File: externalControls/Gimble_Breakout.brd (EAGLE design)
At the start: 33 x 41.6 mm, 5 parts

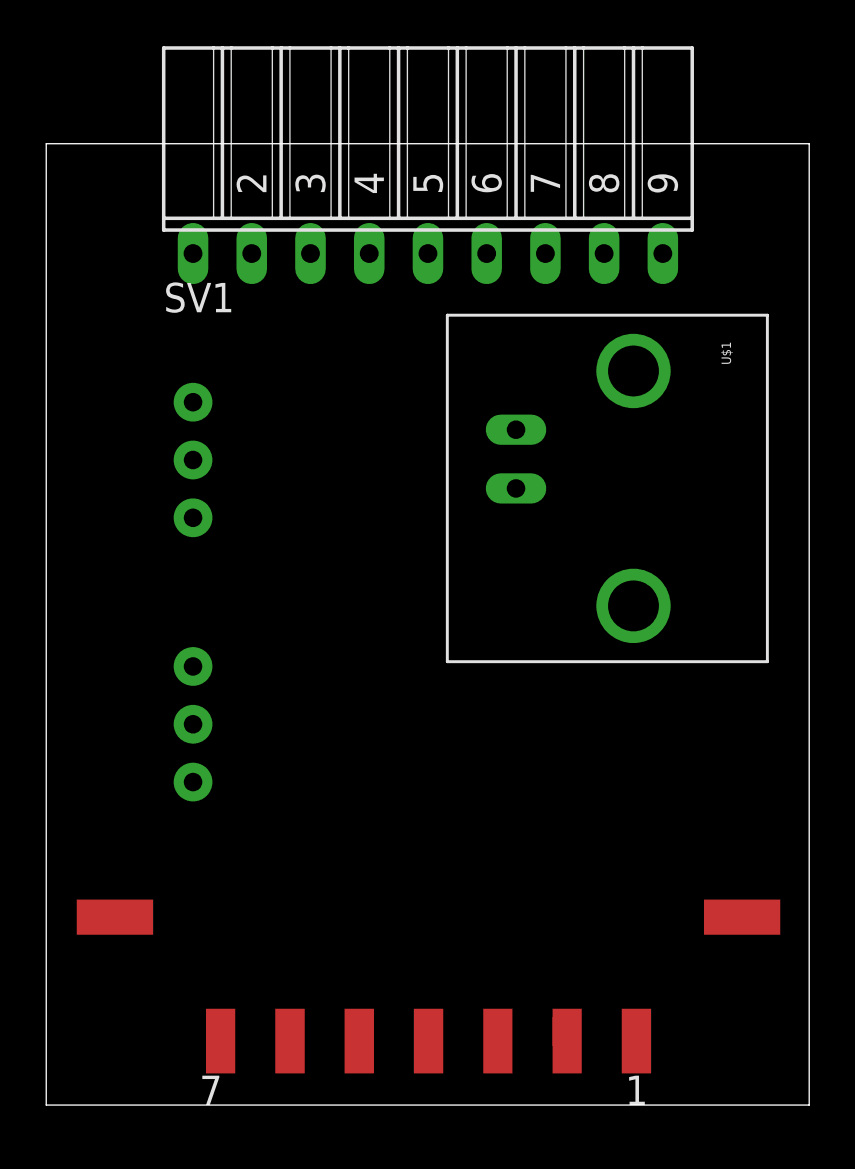
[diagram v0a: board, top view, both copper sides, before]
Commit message: Updated Routing
optimized a few paths
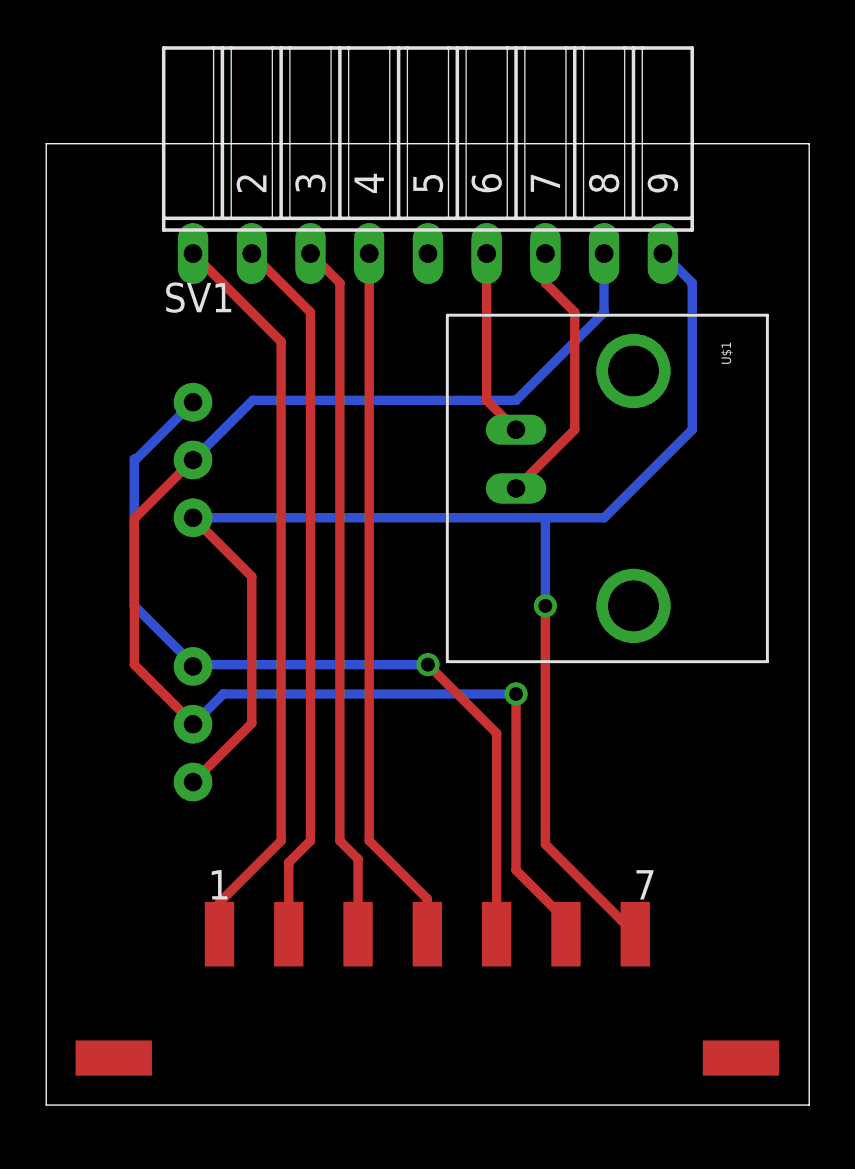
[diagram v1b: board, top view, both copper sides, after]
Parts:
- moved U$2 31.4 mm to (0.00, 59.7), turned to 0 degrees
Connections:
- net +12V: now also U$2.6
- net CAM_PWM0: now also U$2.4
- net CAM_PWM1: now also U$2.3
- net CAM_PWM2: now also U$2.2
- net CAM_PWM3: now also U$2.PAD1
- net DYNA_DATA: now also U$2.5
- net GND: now also U$2.7
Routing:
- net GND: track 0.00 -> 64.5 mm, vias 0 -> 1
- net +12V: track 0.00 -> 62.3 mm, vias 0 -> 1
- net DYNA_DATA: track 0.00 -> 36.7 mm, vias 0 -> 1
- net CAM_PWM3: track 0.00 -> 32.1 mm
- net CAM_PWM2: track 0.00 -> 30.9 mm
- net CAM_PWM0: track 0.00 -> 30.5 mm
- net CAM_PWM1: track 0.00 -> 30.3 mm
- net CAM_VIDEO: track 0.00 -> 11.7 mm
- net CAM_VIDEO_GND: track 0.00 -> 8.15 mm
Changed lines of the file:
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@@
 </element>
 <element name="U$1" library="SparkFun-Connectors" package="BNC" value="BNCPTH" x="19.05" y="85.09" rot="R270"/>
-<element name="U$2" library="logicShifter" package="MOLEX7PIN" value="MOLEX7-PIN" x="30.48" y="67.31" rot="R180"/>
+<element name="U$2" library="logicShifter" package="MOLEX7PIN" value="MOLEX7-PIN" x="0" y="59.69">
+<attribute name="TEST" value="1" x="0" y="59.69" size="1.778" layer="27" display="off"/>
+</element>
 </elements>
 <signals>
@@
 <contactref element="DYNA1" pad="P$1"/>
 <contactref element="SV1" pad="9"/>
-<wire x1="5.08" y1="83.82" x2="25.4" y2="95.25" width="0" layer="19" extent="1-1"/>
-<wire x1="5.08" y1="72.39" x2="5.08" y2="83.82" width="0" layer="19" extent="1-1"/>
+<contactref element="U$2" pad="7"/>
+<wire x1="5.08" y1="83.82" x2="7.62" y2="81.28" width="0.4064" layer="1"/>
+<wire x1="7.62" y1="81.28" x2="7.62" y2="74.93" width="0.4064" layer="1"/>
+<wire x1="7.62" y1="74.93" x2="5.08" y2="72.39" width="0.4064" layer="1"/>
+<wire x1="25.4" y1="95.25" x2="26.67" y2="93.98" width="0.4064" layer="16"/>
+<wire x1="26.67" y1="93.98" x2="26.67" y2="87.63" width="0.4064" layer="16"/>
+<wire x1="26.67" y1="87.63" x2="22.86" y2="83.82" width="0.4064" layer="16"/>
+<wire x1="22.86" y1="83.82" x2="20.32" y2="83.82" width="0.4064" layer="16"/>
+<wire x1="20.32" y1="83.82" x2="5.08" y2="83.82" width="0.4064" layer="16"/>
+<wire x1="24.2062" y1="65.8114" x2="20.32" y2="69.6976" width="0.4064" layer="1"/>
+<wire x1="20.32" y1="69.6976" x2="20.32" y2="80.01" width="0.4064" layer="1"/>
+<via x="20.32" y="80.01" extent="1-16" drill="0.6"/>
+<wire x1="20.32" y1="80.01" x2="20.32" y2="83.82" width="0.4064" layer="16"/>
 </signal>
 <signal name="+12V">
@@
 <contactref element="DYNA1" pad="P$2"/>
 <contactref element="SV1" pad="8"/>
-<wire x1="5.08" y1="86.32" x2="22.86" y2="95.25" width="0" layer="19" extent="1-1"/>
-<wire x1="5.08" y1="74.89" x2="5.08" y2="86.32" width="0" layer="19" extent="1-1"/>
+<contactref element="U$2" pad="6"/>
+<wire x1="5.08" y1="86.32" x2="2.58" y2="83.82" width="0.4064" layer="1"/>
+<wire x1="2.58" y1="83.82" x2="2.54" y2="83.82" width="0.4064" layer="1"/>
+<wire x1="2.54" y1="83.82" x2="2.54" y2="77.47" width="0.4064" layer="1"/>
+<wire x1="2.54" y1="77.47" x2="5.08" y2="74.93" width="0.4064" layer="1"/>
+<wire x1="5.08" y1="74.93" x2="5.08" y2="74.89" width="0.4064" layer="1"/>
+<wire x1="5.08" y1="86.32" x2="7.66" y2="88.9" width="0.4064" layer="16"/>
+<wire x1="7.66" y1="88.9" x2="19.05" y2="88.9" width="0.4064" layer="16"/>
+<wire x1="19.05" y1="88.9" x2="22.86" y2="92.71" width="0.4064" layer="16"/>
+<wire x1="22.86" y1="92.71" x2="22.86" y2="95.25" width="0.4064" layer="16"/>
+<wire x1="5.08" y1="74.89" x2="6.39" y2="76.2" width="0.4064" layer="16"/>
+<wire x1="6.39" y1="76.2" x2="19.05" y2="76.2" width="0.4064" layer="16"/>
+<via x="19.05" y="76.2" extent="1-16" drill="0.6"/>
+<wire x1="19.05" y1="76.2" x2="19.05" y2="68.58" width="0.4064" layer="1"/>
+<wire x1="19.05" y1="68.58" x2="21.209" y2="66.421" width="0.4064" layer="1"/>
+<wire x1="21.209" y1="66.421" x2="21.209" y2="65.8114" width="0.4064" layer="1"/>
 </signal>
 <signal name="DYNA_DATA">
 <contactref element="DYNA2" pad="P$3"/>
 <contactref element="DYNA1" pad="P$3"/>
-<wire x1="5.08" y1="77.39" x2="5.08" y2="88.82" width="0" layer="19" extent="1-1"/>
+<contactref element="U$2" pad="5"/>
+<wire x1="5.08" y1="88.82" x2="2.62" y2="86.36" width="0.4064" layer="16"/>
+<wire x1="2.62" y1="86.36" x2="2.54" y2="86.36" width="0.4064" layer="16"/>
+<wire x1="2.54" y1="86.36" x2="2.54" y2="80.01" width="0.4064" layer="16"/>
+<wire x1="2.54" y1="80.01" x2="5.08" y2="77.47" width="0.4064" layer="16"/>
+<wire x1="5.08" y1="77.47" x2="5.08" y2="77.39" width="0.4064" layer="16"/>
+<wire x1="5.08" y1="77.39" x2="5.16" y2="77.47" width="0.4064" layer="16"/>
+<wire x1="5.16" y1="77.47" x2="15.24" y2="77.47" width="0.4064" layer="16"/>
+<via x="15.24" y="77.47" extent="1-16" drill="0.6"/>
+<wire x1="15.24" y1="77.47" x2="18.2118" y2="74.4982" width="0.4064" layer="1"/>
+<wire x1="18.2118" y1="74.4982" x2="18.2118" y2="65.8114" width="0.4064" layer="1"/>
 </signal>
 <signal name="NC">
@@
 <contactref element="SV1" pad="7"/>
 <contactref element="U$1" pad="S"/>
-<wire x1="19.05" y1="85.09" x2="20.32" y2="95.25" width="0" layer="19" extent="1-1"/>
+<wire x1="19.05" y1="85.09" x2="21.59" y2="87.63" width="0.4064" layer="1"/>
+<wire x1="21.59" y1="87.63" x2="21.59" y2="92.71" width="0.4064" layer="1"/>
+<wire x1="21.59" y1="92.71" x2="20.32" y2="93.98" width="0.4064" layer="1"/>
+<wire x1="20.32" y1="93.98" x2="20.32" y2="95.25" width="0.4064" layer="1"/>
 </signal>
 <signal name="CAM_VIDEO_GND">
 <contactref element="SV1" pad="6"/>
 <contactref element="U$1" pad="GND"/>
-<wire x1="19.05" y1="87.63" x2="17.78" y2="95.25" width="0" layer="19" extent="1-1"/>
+<wire x1="19.05" y1="87.63" x2="17.78" y2="88.9" width="0.4064" layer="1"/>
+<wire x1="17.78" y1="88.9" x2="17.78" y2="95.25" width="0.4064" layer="1"/>
 </signal>
 <signal name="CAM_PWM3">
 <contactref element="SV1" pad="1"/>
+<contactref element="U$2" pad="PAD1"/>
+<wire x1="5.08" y1="95.25" x2="8.89" y2="91.44" width="0.4064" layer="1"/>
+<wire x1="8.89" y1="91.44" x2="8.89" y2="69.85" width="0.4064" layer="1"/>
+<wire x1="8.89" y1="69.85" x2="6.223" y2="67.183" width="0.4064" layer="1"/>
+<wire x1="6.223" y1="67.183" x2="6.223" y2="65.8114" width="0.4064" layer="1"/>
 </signal>
 <signal name="CAM_PWM2">
 <contactref element="SV1" pad="2"/>
+<contactref element="U$2" pad="2"/>
+<wire x1="7.62" y1="95.25" x2="10.16" y2="92.71" width="0.4064" layer="1"/>
+<wire x1="10.16" y1="92.71" x2="10.16" y2="69.85" width="0.4064" layer="1"/>
+<wire x1="10.16" y1="69.85" x2="9.2202" y2="68.9102" width="0.4064" layer="1"/>
+<wire x1="9.2202" y1="68.9102" x2="9.2202" y2="65.8114" width="0.4064" layer="1"/>
 </signal>
 <signal name="CAM_PWM1">
 <contactref element="SV1" pad="3"/>
+<contactref element="U$2" pad="3"/>
+<wire x1="10.16" y1="95.25" x2="11.43" y2="93.98" width="0.4064" layer="1"/>
+<wire x1="11.43" y1="93.98" x2="11.43" y2="69.85" width="0.4064" layer="1"/>
+<wire x1="11.43" y1="69.85" x2="12.2174" y2="69.0626" width="0.4064" layer="1"/>
+<wire x1="12.2174" y1="69.0626" x2="12.2174" y2="65.8114" width="0.4064" layer="1"/>
 </signal>
 <signal name="CAM_PWM0">
 <contactref element="SV1" pad="4"/>
+<contactref element="U$2" pad="4"/>
+<wire x1="12.7" y1="95.25" x2="12.7" y2="69.85" width="0.4064" layer="1"/>
+<wire x1="12.7" y1="69.85" x2="15.2146" y2="67.3354" width="0.4064" layer="1"/>
+<wire x1="15.2146" y1="67.3354" x2="15.2146" y2="65.8114" width="0.4064" layer="1"/>
 </signal>
 </signals>
